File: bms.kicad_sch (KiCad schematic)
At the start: 64 parts, among them J1 Screw_Terminal_01x02, J2 Molex_Pico-Clasp_1x7_Horizont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, Q1 CSD17579Q5A, Q10 DMG2301L, Q12 DMN2056U, Q2 CSD17579Q5A, Q3 SiA453EDJ, Q4 Si1442DH, Q5 DMN2056U, Q7 2N7002K, Q8 DMN2056U, U1 BQ40Z50RSMT-R2, U2 BQ29410_TSSOP

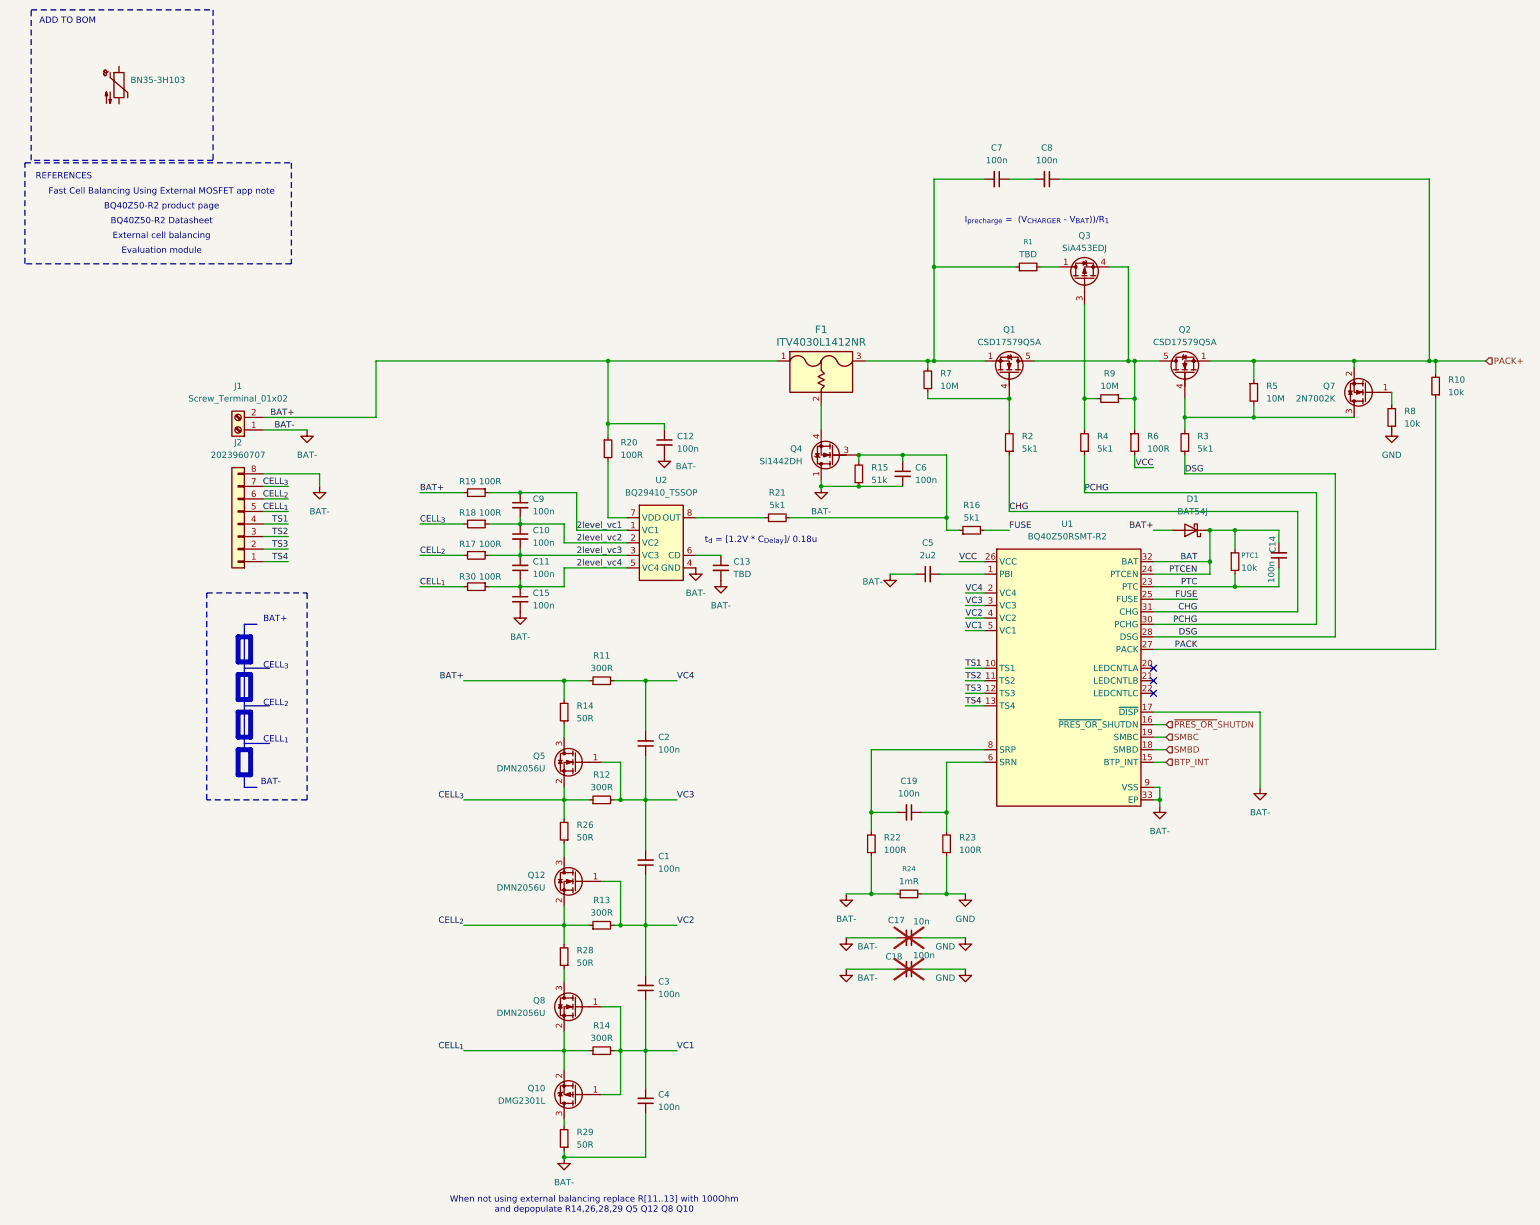
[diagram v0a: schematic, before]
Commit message: Export footprints, symbols into a common library
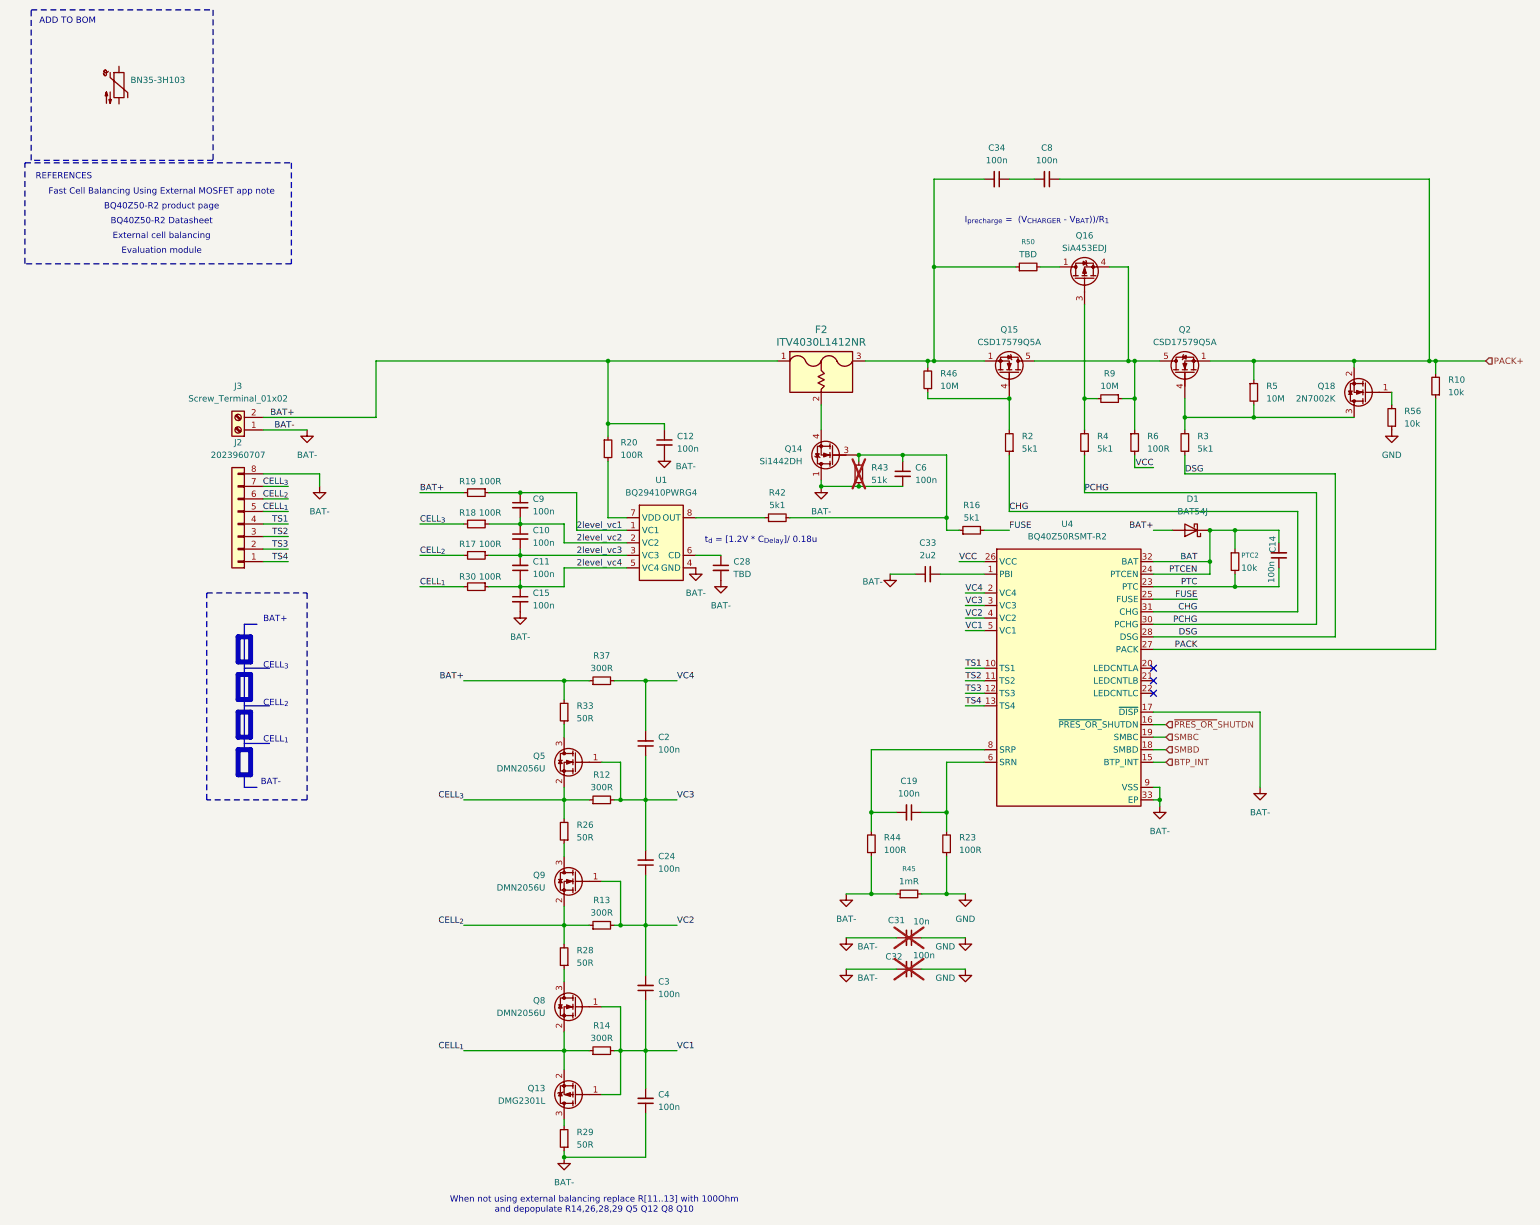
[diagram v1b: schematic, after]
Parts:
- removed U2: BQ29410_TSSOP, Hardware Components Footprints:TSSOP-8_3x4.4mm_P0.65mm, symbol Hardware Components:BQ29410_TSSOP
- added U1: BQ29410_TSSOP, Hardware Components Footprints:TSSOP-8_3x4.4mm_P0.65mm, symbol bq29410_tssop:BQ29410_TSSOP
- C10, C11, C12, C14, C15, C19, C2, C3, C4, C6, C9: footprint Hardware Components Footprints:C_0402_1005Metric -> Capacitor_SMD:C_0402_1005Metric
- C24: renamed from C1; footprint Hardware Components Footprints:C_0402_1005Metric -> Capacitor_SMD:C_0402_1005Metric
- C31: renamed from C17; footprint Hardware Components Footprints:C_0402_1005Metric -> Capacitor_SMD:C_0402_1005Metric
- C32: renamed from C18; footprint Hardware Components Footprints:C_0402_1005Metric -> Capacitor_SMD:C_0402_1005Metric
- C33: renamed from C5; footprint Hardware Components Footprints:C_0603_1608Metric -> Capacitor_SMD:C_0603_1608Metric
- C34: renamed from C7; footprint Hardware Components Footprints:C_0603_1608Metric -> Capacitor_SMD:C_0603_1608Metric
- C8: footprint Hardware Components Footprints:C_0603_1608Metric -> Capacitor_SMD:C_0603_1608Metric
- R10, R12, R13, R14, R16, R17, R18, R19, R2, R20, R23, R26, R28, R29, R3, R30, R4, R5, R6, R9: footprint Hardware Components Footprints:R_0402_1005Metric -> Resistor_SMD:R_0402_1005Metric
- R33: renamed from R14; footprint Hardware Components Footprints:R_0402_1005Metric -> Resistor_SMD:R_0402_1005Metric
- R37: renamed from R11; footprint Hardware Components Footprints:R_0402_1005Metric -> Resistor_SMD:R_0402_1005Metric
- R42: renamed from R21; footprint Hardware Components Footprints:R_0402_1005Metric -> Resistor_SMD:R_0402_1005Metric
- R43: renamed from R15; footprint Hardware Components Footprints:R_0402_1005Metric -> Resistor_SMD:R_0402_1005Metric; now not fitted
- R44: renamed from R22; footprint Hardware Components Footprints:R_0402_1005Metric -> Resistor_SMD:R_0402_1005Metric
- R46: renamed from R7; footprint Hardware Components Footprints:R_0402_1005Metric -> Resistor_SMD:R_0402_1005Metric
- R56: renamed from R8; footprint Hardware Components Footprints:R_0402_1005Metric -> Resistor_SMD:R_0402_1005Metric
- U4: renamed from U1; footprint BQ40Z50RSMTR2 -> UserLib:BQ40Z50RSMTR2
- renumbered C13 to C28, F1 to F2, J1 to J3, PTC1 to PTC2, Q10 to Q13, Q4 to Q14, Q1 to Q15, Q3 to Q16, Q7 to Q18, Q12 to Q9, R24 to R45, R1 to R50, xx to xx1
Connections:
- net 2level_vc1: now also U1.1 (VC1)
- net 2level_vc2: now also U1.2 (VC2)
- net 2level_vc3: now also U1.3 (VC3)
- net 2level_vc4: now also U1.5 (VC4)
- net BAT-: now also U1.4 (GND)
- net at C28.1: now also U1.6 (CD)
- net at R20.2: now also U1.7 (VDD)
- net at R42.1: now also U1.8 (OUT)
